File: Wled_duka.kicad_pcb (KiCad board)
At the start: 2 copper layers, 100 x 100 mm, 40 parts, among them J1 7775-2, J2 DATA channels, J3 CH1&2, J4 CH3&4, J5 Relay out, J6 DMX512, J7 7775-2, Q1 AO3400A, U1 XL1509-5.0, U2 ESP32_S3_supermini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

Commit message: V2
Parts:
- added J8: Vin_alt, Connector_PinHeader_2.54mm:PinHeader_1x02_P2.54mm_Vertical, F.Cu at (131.6, 122.9)
- moved D2 3.75 mm to (128.3, 132.7), turned to 90 degrees
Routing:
- net Vin: track 0.14 -> 38.8 mm
- net V12: track 26.9 -> 32.9 mm
- net Net-(J4-Pin_4): vias 0 -> 27
- net Net-(J4-Pin_2): vias 0 -> 28
- net Net-(J3-Pin_4): vias 0 -> 27
- net Net-(J3-Pin_2): vias 0 -> 27
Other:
- board text added: "+"
- board text added: "+12V"
- board text added: "-"
- board text added: "Cut here if you don't need FUSES -->"
- board text added: "Relay out"
- board text added: "Use ATO (normal) size FUSES! It can work with 9-24V DC."
- board text added: "Use automotiv relay!!!"

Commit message: LDO
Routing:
- net Net-(D1-K): track 11.0 -> 0.21 mm
- added copper zone on F.Cu, net Net-(D1-K)
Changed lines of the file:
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@@
-	)
-	(segment
-		(start 142.8175 124.075)
-		(end 142.8175 122.437486)
-		(width 1)
-		(layer "F.Cu")
-		(net "Net-(D1-K)")
 	)
 	(segment
@@
 	)
 	(segment
-		(start 146.4 118.6575)
-		(end 146.4 114.5575)
-		(width 1)
-		(layer "F.Cu")
-		(net "Net-(D1-K)")
-	)
-	(segment
-		(start 144.8825 120.175)
-		(end 146.4 118.6575)
-		(width 1)
-		(layer "F.Cu")
-		(net "Net-(D1-K)")
-	)
-	(segment
 		(start 144.8825 120.372486)
 		(end 144.8825 120.175)
-		(width 1)
-		(layer "F.Cu")
-		(net "Net-(D1-K)")
-	)
-	(segment
-		(start 142.8175 122.437486)
-		(end 144.8825 120.372486)
 		(width 1)
 		(layer "F.Cu")
@@
 			)
 		)
+	)
+	(zone
+		(net "Net-(D1-K)")
+		(layer "F.Cu")
+		(hatch edge 0.5)
+		(priority 4)
+		(connect_pads yes
+			(clearance 0.5)
+		)
+		(min_thickness 0.25)
+		(fill yes
+			(thermal_gap 0.5)
+			(thermal_bridge_width 0.5)
+			(smoothing fillet)
+			(radius 2)
+			(island_removal_mode 1)
+		)
+		(polygon
+			(pts
+				(xy 143.325 125.075) (xy 143.325 122.675) (xy 146.95 121.75) (xy 147.55 117.225) (xy 147.55 111.775)
+				(xy 145.225 111.775) (xy 145.225 117.4) (xy 143.3 120.775) (xy 142.325 121.7) (xy 142.3 125.075)
+			)
+		)

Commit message: GND fix
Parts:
- moved J7 3.70 mm to (100.9, 131.9)
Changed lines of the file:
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@@
 	(footprint "screw pin:77752"
 		(layer "F.Cu")
-		(at 101 128.23)
+		(at 100.9 131.925)
 		(descr "7775-2-3")
 		(tags "Connector")
@@
 	)
 	(gr_text "GND"
-		(at 86.928572 127.375 0)
+		(at 86.7 129.975 0)
 		(layer "F.SilkS")
 		(effects

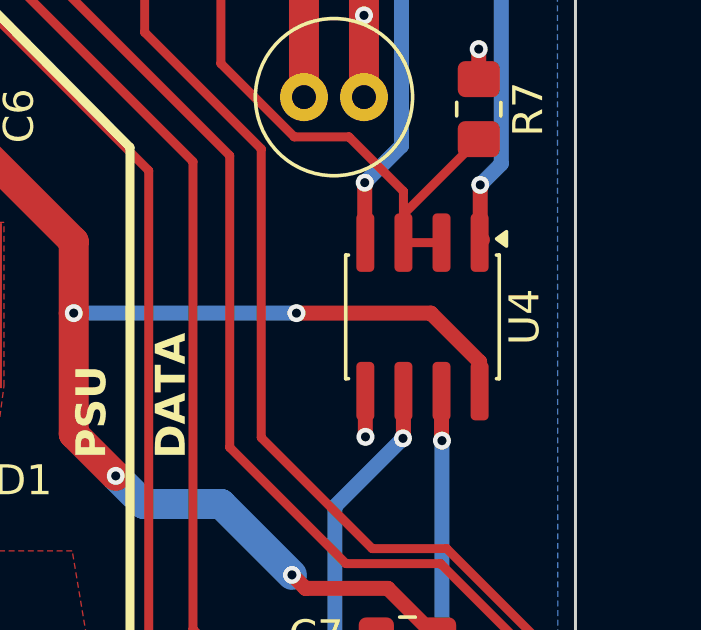
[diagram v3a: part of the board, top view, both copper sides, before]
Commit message: Max485 remove --- Max3485 placed
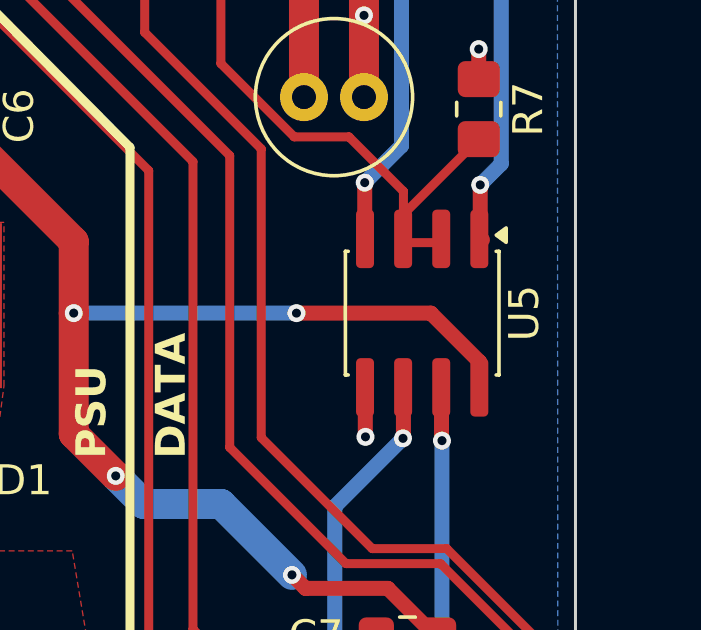
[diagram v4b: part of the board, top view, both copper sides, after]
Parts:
- removed U4: MAX485E, Package_SO:SOIC-8_3.9x4.9mm_P1.27mm
- added U5: MAX3485, Package_SO:SOIC-8_3.9x4.9mm_P1.27mm, F.Cu at (161.5, 114.8)

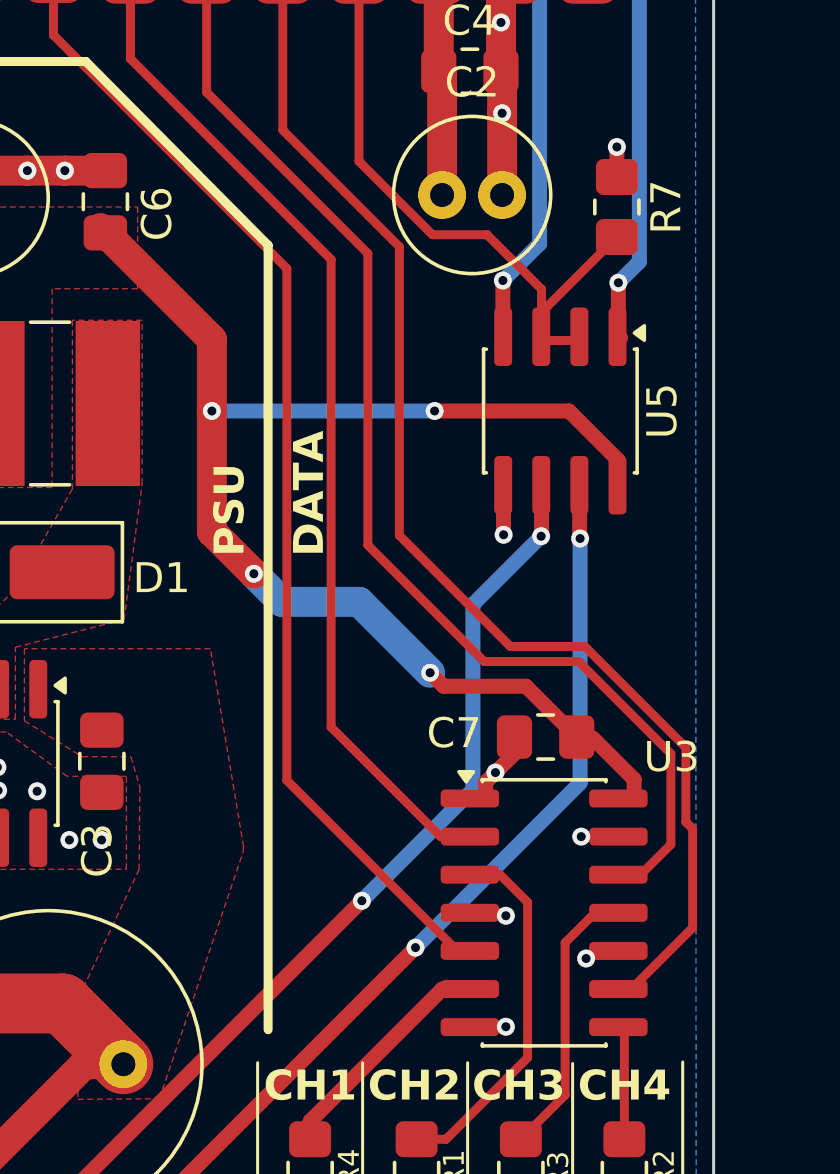
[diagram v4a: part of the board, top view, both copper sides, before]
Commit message: Pullup and Pulldown resistors, 3,3V for max3485
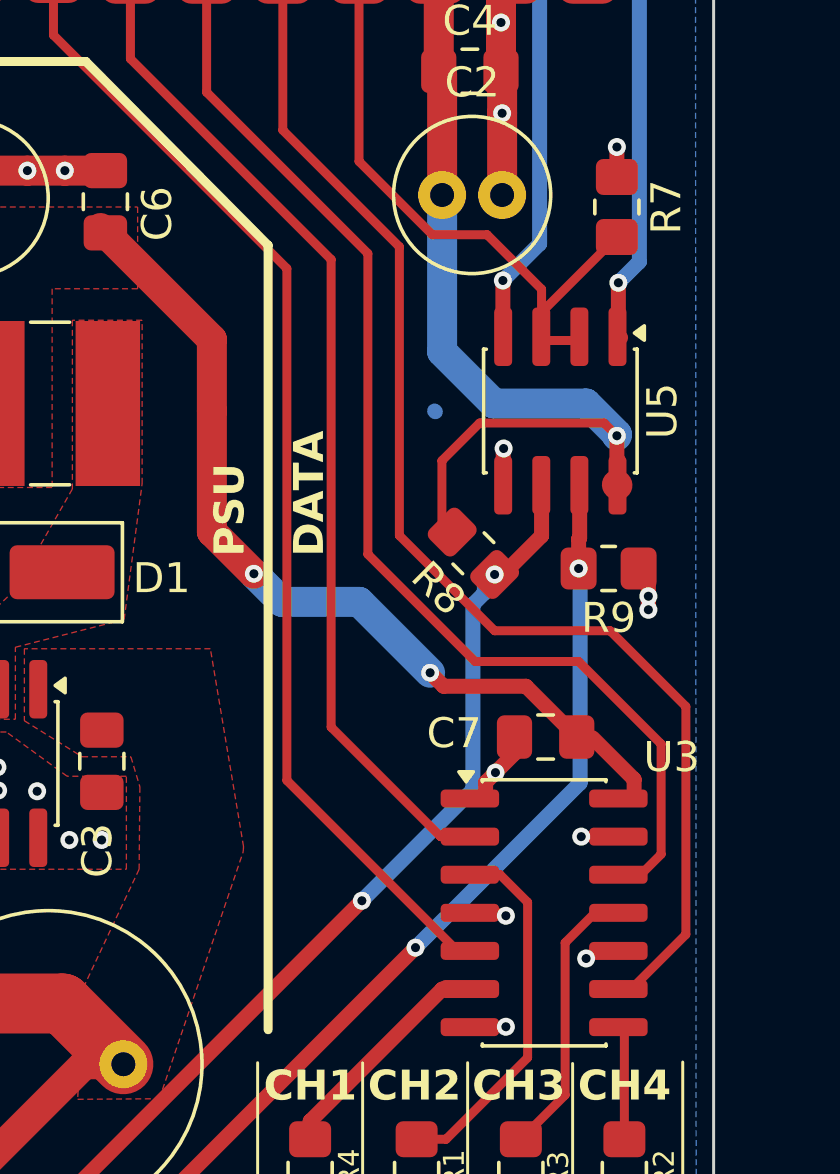
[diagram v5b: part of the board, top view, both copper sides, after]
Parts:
- added R8: 10k, Resistor_SMD:R_0805_2012Metric_Pad1.20x1.40mm_HandSolder, F.Cu at (158.6, 119.5)
- added R9: 10k, Resistor_SMD:R_0805_2012Metric_Pad1.20x1.40mm_HandSolder, F.Cu at (163.1, 120.0)
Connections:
- C2 pad 1: Net-(U2-3,3V) -> +3,3V
- C4 pad 1: Net-(U2-3,3V) -> +3,3V
- U2 pad 16: Net-(U2-3,3V) -> +3,3V
- U5 pad 8: +5V -> +3,3V
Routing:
- net +3,3V: track 0.00 -> 31.5 mm, vias 0 -> 1
- net +5V: track 91.3 -> 76.1 mm, vias 4 -> 2
- net Net-(U2-3,3V): track 7.97 -> 0.00 mm
- net GND: track 27.4 -> 29.0 mm, vias 27 -> 29
- net IO_ch4: track 42.7 -> 43.3 mm
